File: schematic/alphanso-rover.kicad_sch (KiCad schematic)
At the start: 11 parts, among them M1 TT Motor (Adafruit #3777), M2 TT Motor (Adafruit #3777), M3 TT Motor (Adafruit #3777), M4 TT Motor (Adafruit #3777), U1 ESP32-DEVKIT-V1, U2 TB6612FNG, U3 TB6612FNG, U4 LM2596S-5

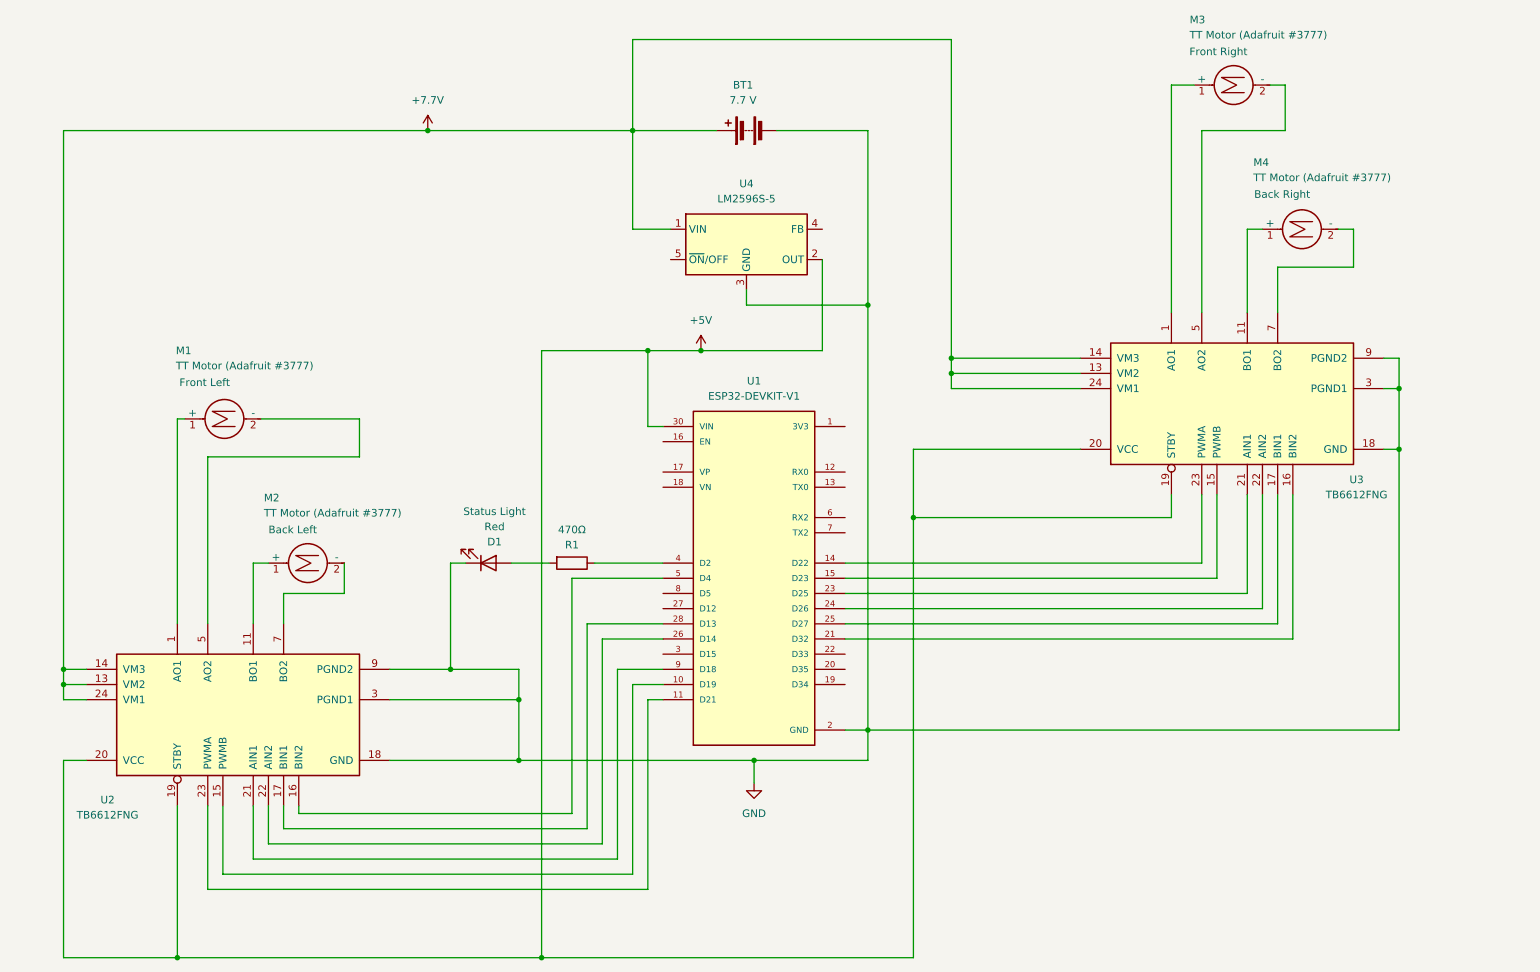
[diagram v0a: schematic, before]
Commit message: updated power net schematics
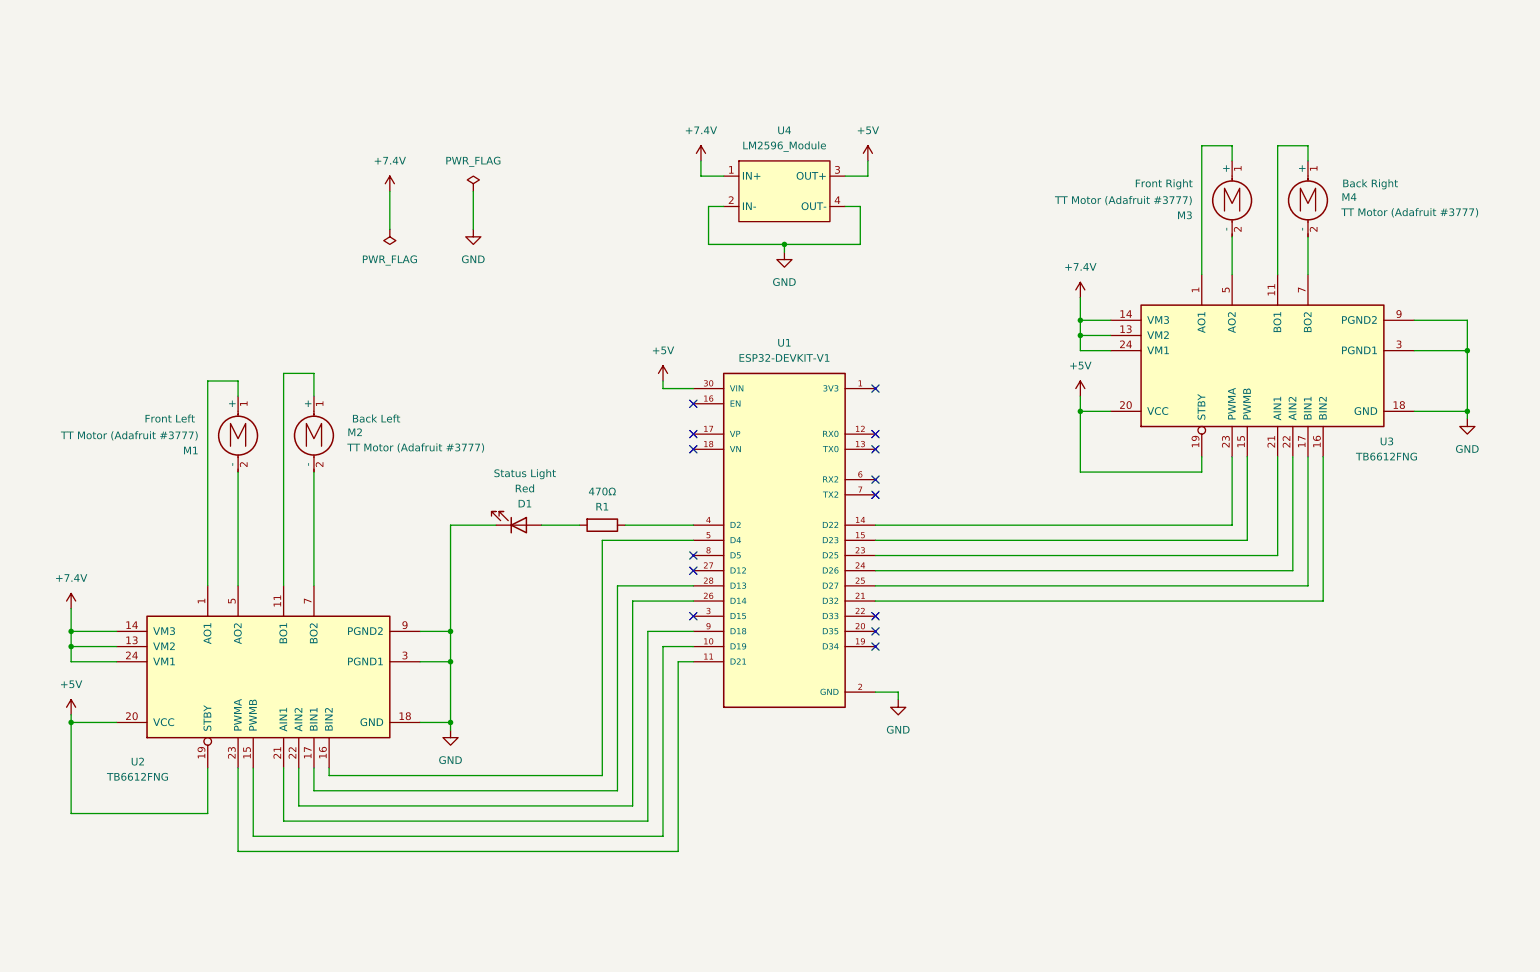
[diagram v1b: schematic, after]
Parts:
- removed BT1: 7.7 V, symbol Device:Battery
- removed U4: LM2596S-5, Package_TO_SOT_SMD:TO-263-5_TabPin3, symbol Regulator_Switching:LM2596S-5
- added U4: LM2596_Module, symbol 1_VoltageRegulators:LM2596_Module
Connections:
- net +5V: now also U4.3 (OUT+)
- net GND: now also U4.2 (IN-), U4.4 (OUT-)
- net +7.7V renamed +7.4V
- net +7.4V: now also U4.1 (IN+)
- no-connect marks 0 -> 14
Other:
- moved on the sheet: D1, M1, M2, R1, U1, U2, U3
